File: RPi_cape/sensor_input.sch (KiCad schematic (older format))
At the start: 39 parts, among them U4 DNP, U5 LM2903, U6 LMC7101B, U7 LMC7101B

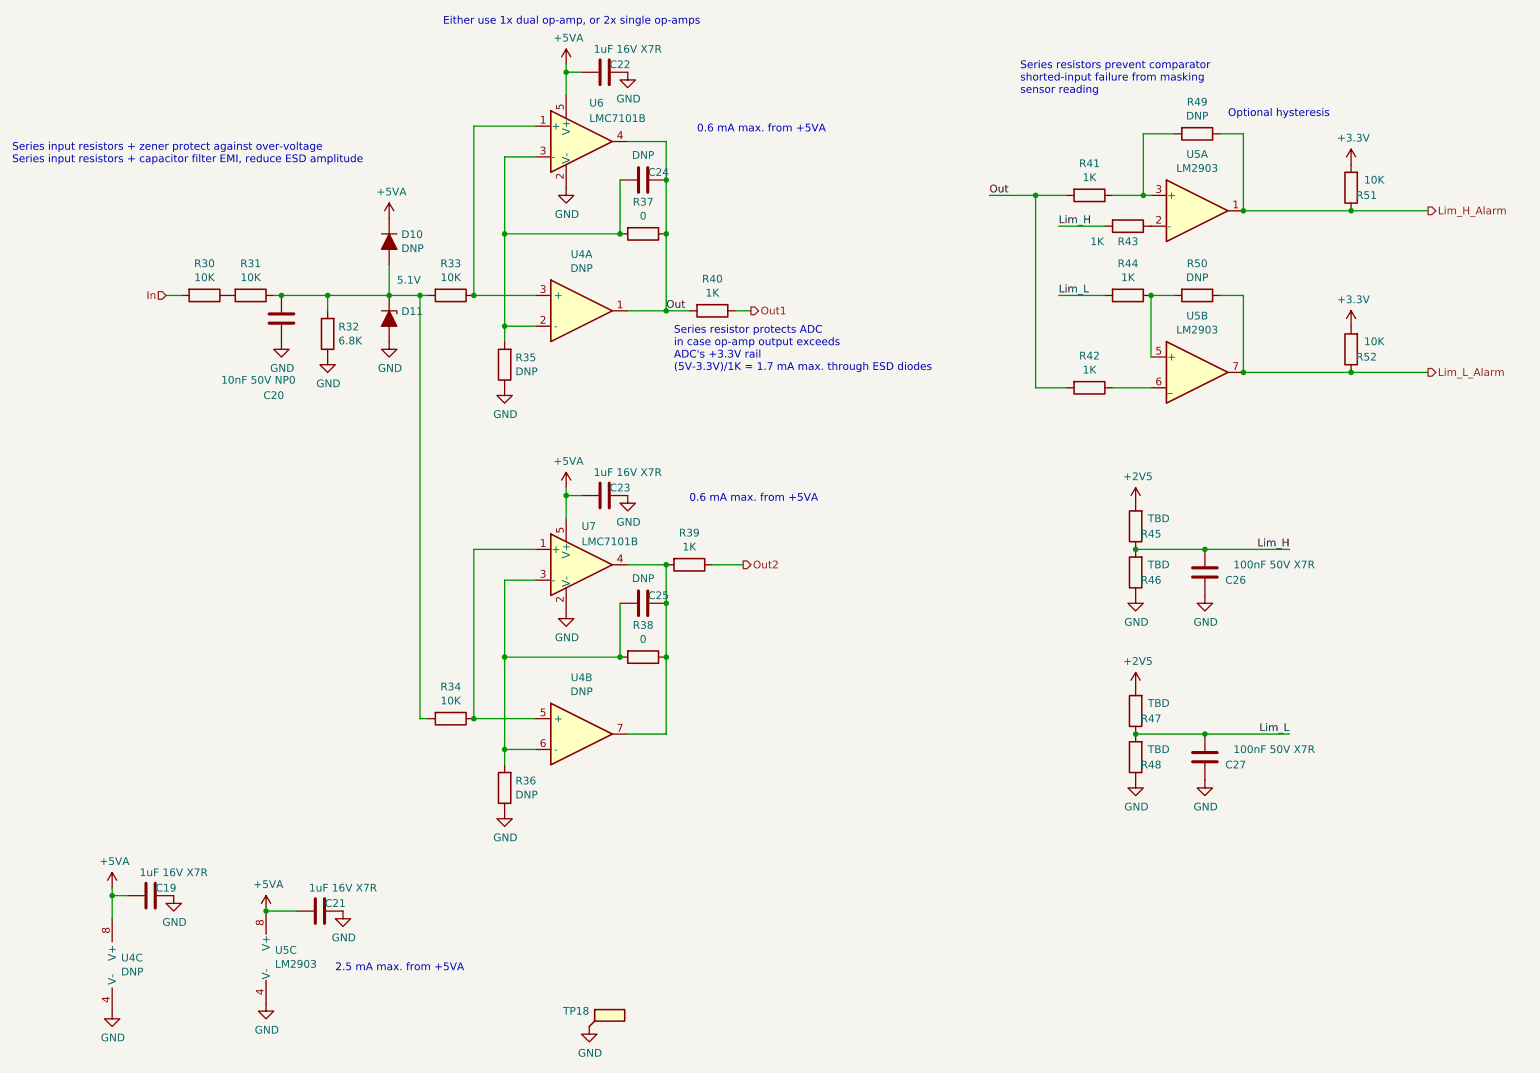
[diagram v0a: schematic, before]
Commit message: Extra info, post-design-review fixes
Added extra info on existing alternate circuit options
Added extra info on parts selection
Created initial PCB file
Added bulk cap to +5V input
Design review fixes:
Moved Raspberry Pi PWM output to GPIO18 to take advantage of hardware PWM
Fixed floating shutdown input on audio amp
Added series resistor R177 to allow low battery output to signal to both CPLD and external LED at the same time
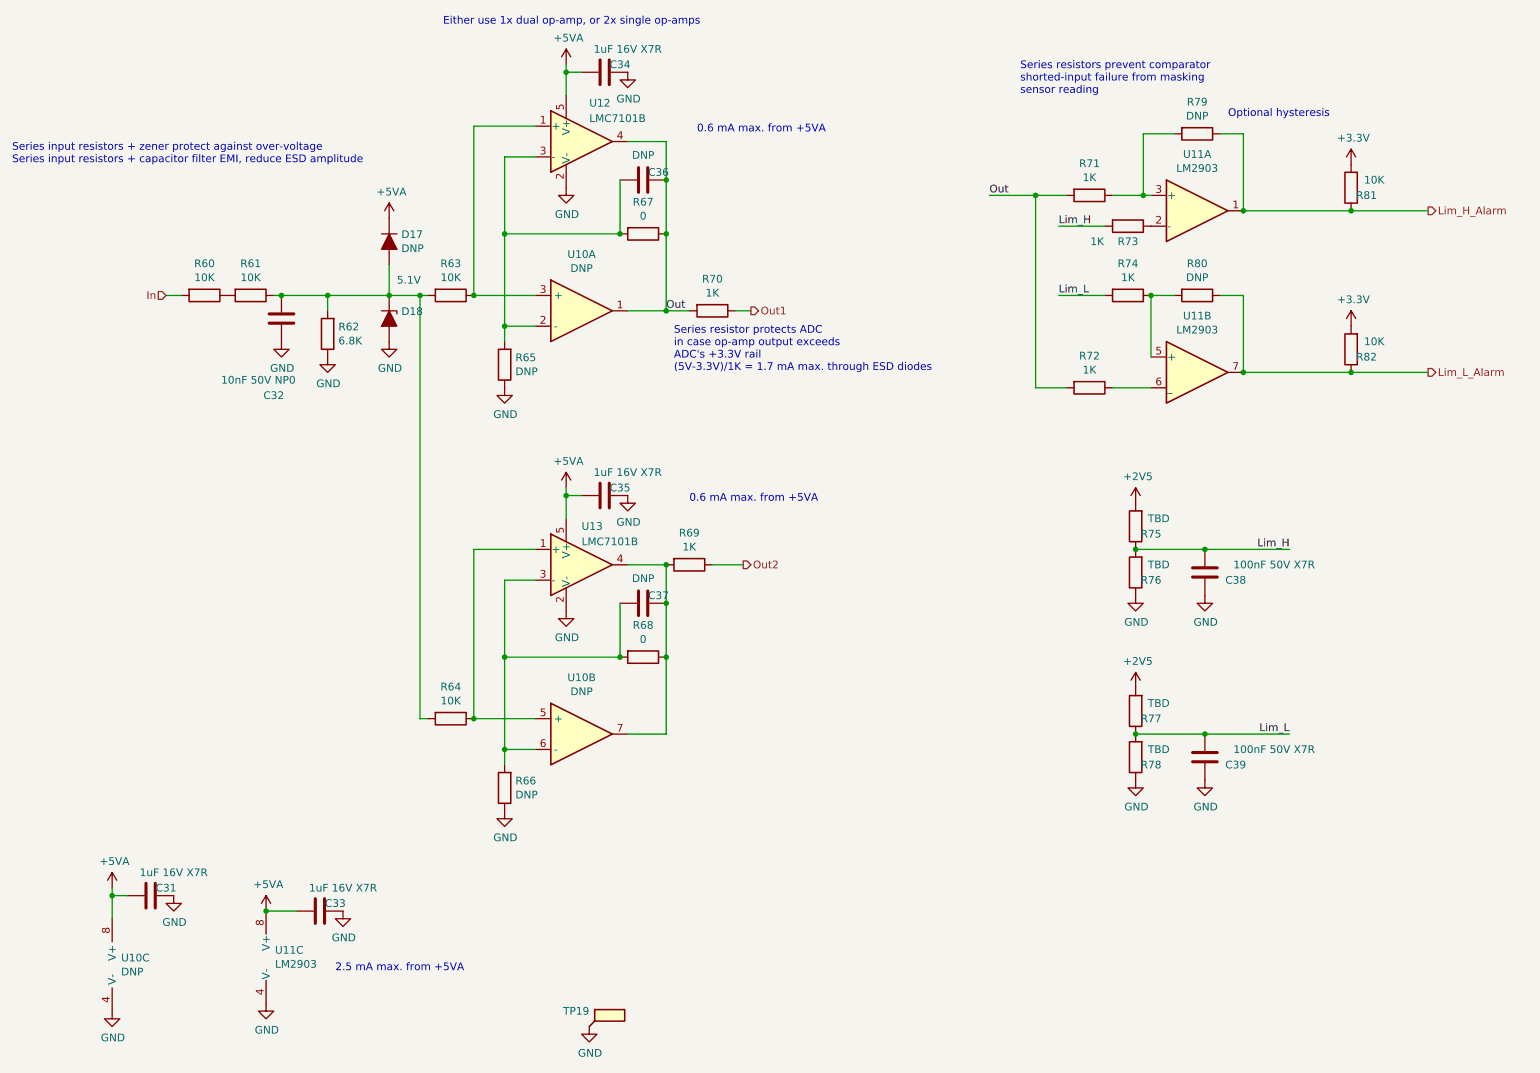
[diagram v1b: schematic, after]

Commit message: Finished schematic, most of PCB placement
Added error budget for analog inputs
Finished most of PCB placement and started routing
Added R185, R186 to allow powering CPLD from alarm power for better power-down alarm sound flexibility
Changed power-down alarm monitoring from +5VD to +3.3V, and put +5VA and +24VA monitoring as DNP by default, to match the CPLD's ability to run off backup battery and monitor +5VA/+24VA
Moved from 3x AA (4.5V) to 4x AA (6V) alarm battery for better audio voltage, and added PNP diode-ORing circuit (Q12 etc.) to accomodate higher voltage, changed low-battery threshold to 5V
Added pull-down resistors to sensor op-amp outputs to help extend low-end output range
Changed 1nF, 10nF, 100nF caps to 0603-size for better fit of CPLD decoupling caps
Added additional bulk cap C19 to audio amp's supply just in case of alarm-induced supply fluctuations
Decreased CPLD's I2C pull-up values to deal with anticipated PCB capacitance etc.
Removed additional dual-op-amp footprint option on analog inputs, due to high availability of single op-amps
Adjusted O2 sensor input clamping to reduce errors from diode leakage current (changed from zener to low-leakage clamps to rails)
Changed O2 sensor op-amp to different lower-offset part to reduce total error from +/- 4.2% FS to +/- 1.7% FS
Fixed missing power section for U17
Added rotary encoder input
Consolidated +5VA fuse options
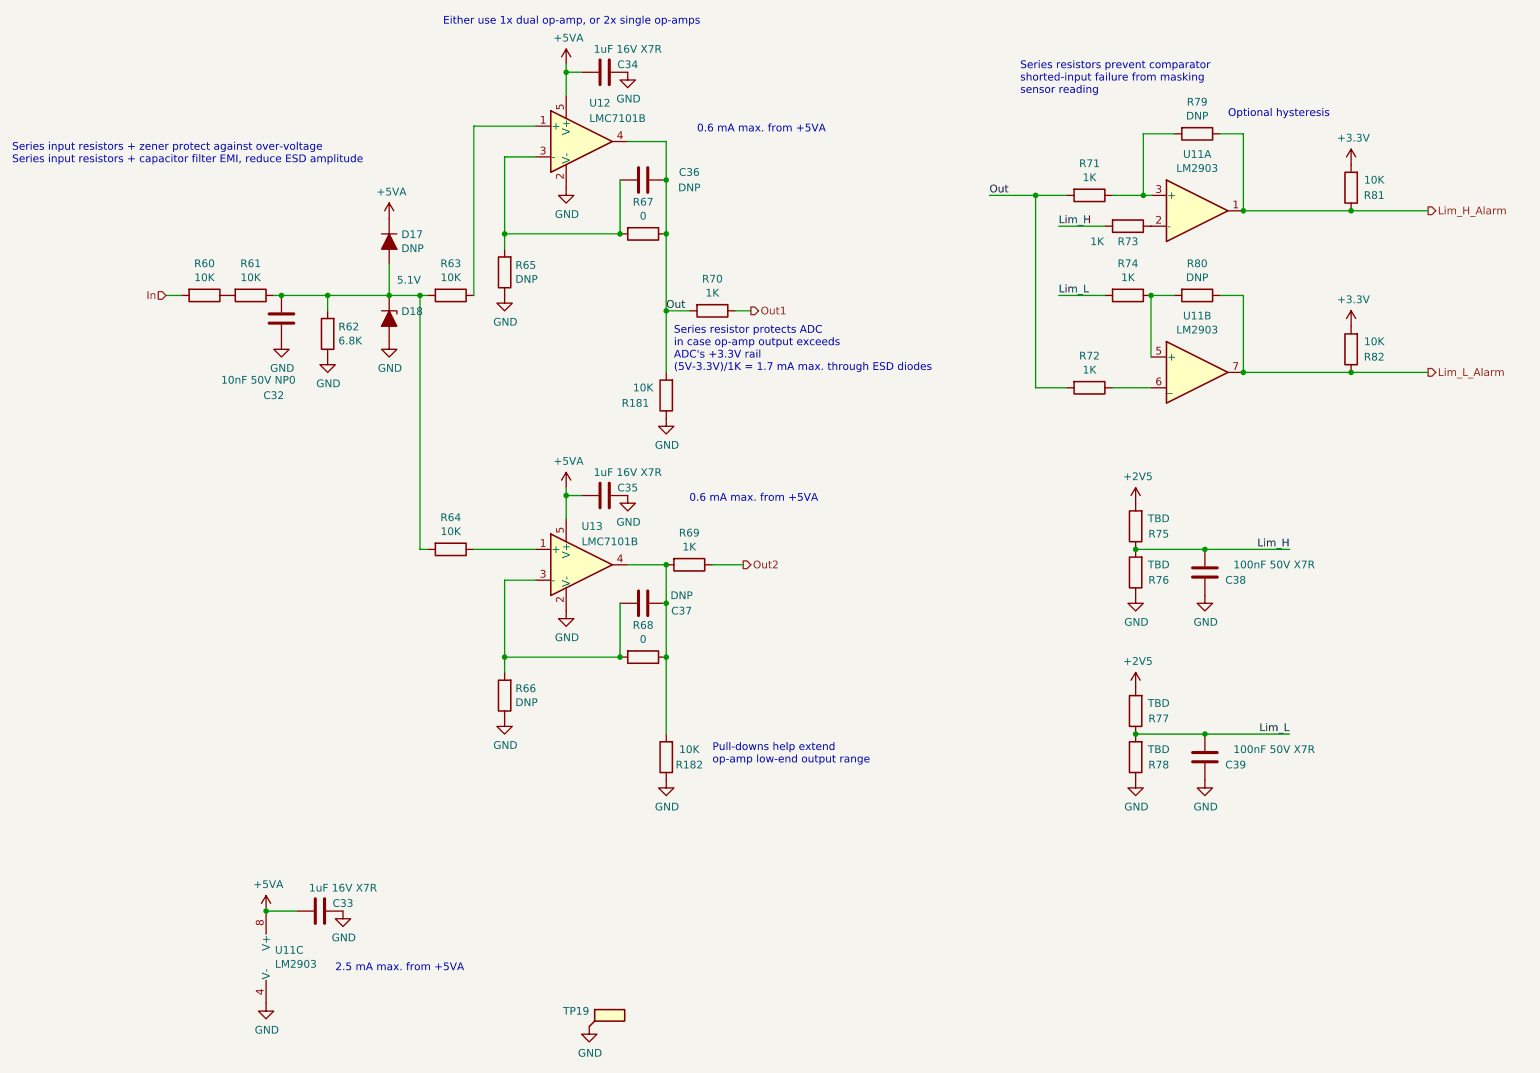
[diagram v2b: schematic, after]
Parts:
- removed C19: 1uF 16V X7R, Capacitor_SMD:C_0805_2012Metric, symbol Device:C
- removed U4: DNP, Package_SO:SOIC-8_3.9x4.9mm_P1.27mm, symbol Device:Opamp_Dual_Generic
- added R179, R180: 10K, Resistor_SMD:R_1206_3216Metric, symbol Device:R
- C20: footprint Capacitor_SMD:C_0805_2012Metric -> Capacitor_SMD:C_0603_1608Metric; Manufacturer Samsung -> Murata; Part Number CL21C103JBFNNNG -> GRM1885C1H103JA01D
- C26, C27: footprint Capacitor_SMD:C_0805_2012Metric -> Capacitor_SMD:C_0603_1608Metric; Part Number 08055C104KAT2A -> 06035C104JAT2A
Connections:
- net GND: now also R179.1, R180.1
- net Out: now also R179.2
- net at C25.1, R38.1, R39.2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: now also R180.2
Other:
- note added: "Pull-downs help extend\nop-amp low-end output range"
- moved on the sheet: R64, R65, R66
